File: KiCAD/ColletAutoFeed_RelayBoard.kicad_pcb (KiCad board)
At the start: 2 copper layers, 117.2 x 159.5 mm, 55 parts, among them J1 XW4M-10D2-H1DS, J2 XW4M-02D1-H1DA, K1 G5V-1, K2 G5V-1, K3 G5V-1, K4 G5V-1, K5 G5V-1, K6 G5V-1, K7 G5V-1, K8 G5V-1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

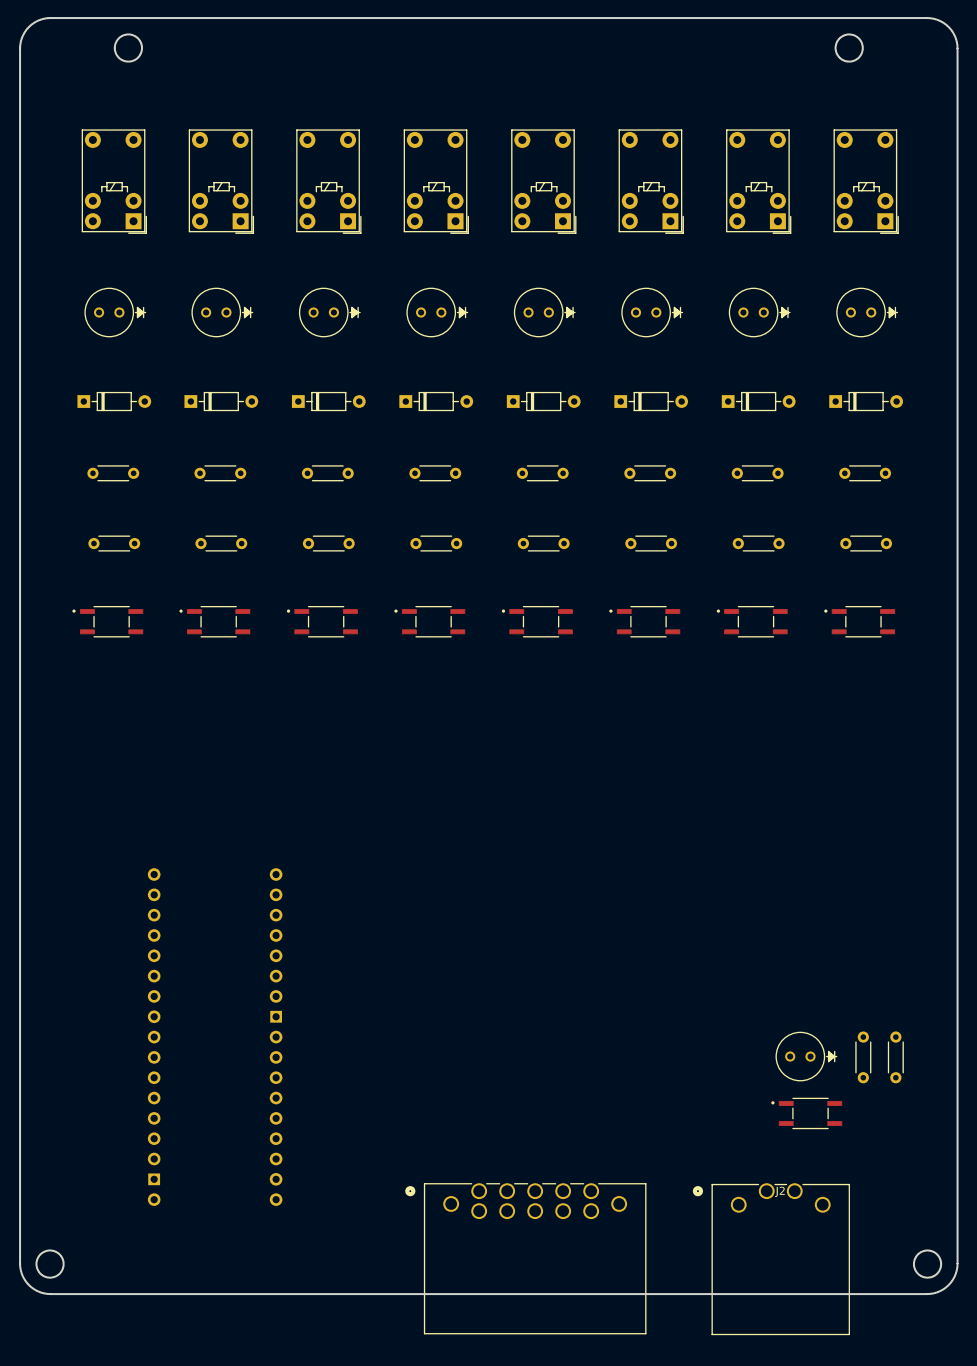
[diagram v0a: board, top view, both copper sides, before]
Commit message: Placed components and routed traces on PCB
Placed components and completed initial routing. Still need to add power and ground planes and figure out silkscreen.
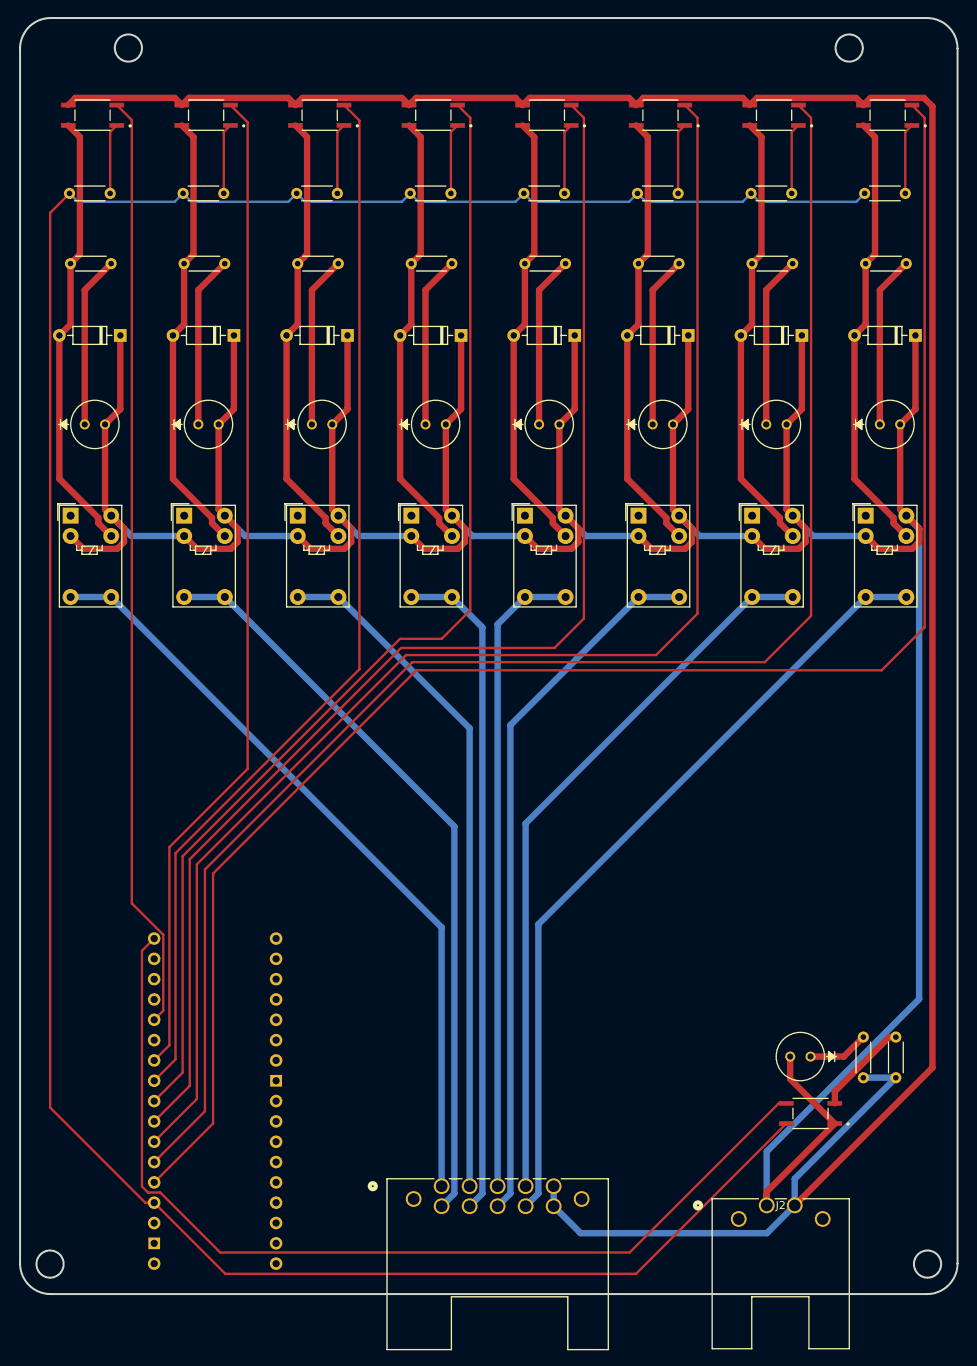
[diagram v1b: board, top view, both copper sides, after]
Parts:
- moved U9 63.4 mm to (143.2, 35.3), turned to 180 degrees
- moved U2 63.4 mm to (43.9, 35.3), turned to 180 degrees
- moved U8 63.4 mm to (129.0, 35.3), turned to 180 degrees
- moved U3 63.3 mm to (58.1, 35.3), turned to 180 degrees
- moved U7 63.3 mm to (114.8, 35.3), turned to 180 degrees
- moved U4 63.3 mm to (72.3, 35.3), turned to 180 degrees
- moved U6 63.3 mm to (100.7, 35.3), turned to 180 degrees
- moved U5 63.3 mm to (86.5, 35.3), turned to 180 degrees
- moved R1 44.5 mm to (41.0, 45.0), turned to 0 degrees
- moved R3 44.4 mm to (55.2, 45.0), turned to 0 degrees
- moved R5 44.3 mm to (69.4, 45.0), turned to 0 degrees
- moved R7 44.1 mm to (83.6, 45.0), turned to 0 degrees
- moved R9 44.1 mm to (97.8, 45.0), turned to 0 degrees
- moved R11 44.0 mm to (112.0, 45.0), turned to 0 degrees
- moved R13 43.9 mm to (126.2, 45.0), turned to 0 degrees
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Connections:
- J1 pad 2: /S2 -> /S3
- J1 pad 3: /S3 -> /S5
- J1 pad 4: /S4 -> /S7
- J1 pad 5: /S5 -> GND
- J1 pad 6: /S6 -> /S2
- J1 pad 7: /S7 -> /S4
- J1 pad 8: /S8 -> /S6
- J1 pad 9: +24V -> /S8
- U2 pad 2: /IO1 -> /IO16
- U3 pad 2: /IO2 -> /IO0
- U4 pad 2: /IO3 -> /IO21
- U5 pad 2: /IO4 -> /IO5
- U6 pad 2: /IO5 -> /IO4
- U7 pad 2: /IO21 -> /IO3
- U8 pad 2: /IO0 -> /IO2
- U9 pad 2: /IO16 -> /IO1
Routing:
- net +24V: track 0.00 -> 472.7 mm
- net /MCU 3.3v: track 0.00 -> 329.1 mm
- net GND: track 0.00 -> 319.3 mm
- net /IO1: track 0.00 -> 209.3 mm
- net /IO2: track 0.00 -> 192.6 mm
- net /IO3: track 0.00 -> 176.7 mm
- net /IO4: track 0.00 -> 161.2 mm
- net /IO5: track 0.00 -> 144.6 mm
- net /IO21: track 0.00 -> 133.4 mm
- net /IO0: track 0.00 -> 125.2 mm
- net /IO12: track 0.00 -> 123.3 mm
- net /IO16: track 0.00 -> 117.2 mm
- net /S8: track 0.00 -> 98.8 mm
- net /S1: track 0.00 -> 95.8 mm
- net /S2: track 0.00 -> 93.8 mm
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
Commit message: Added ground and power planes
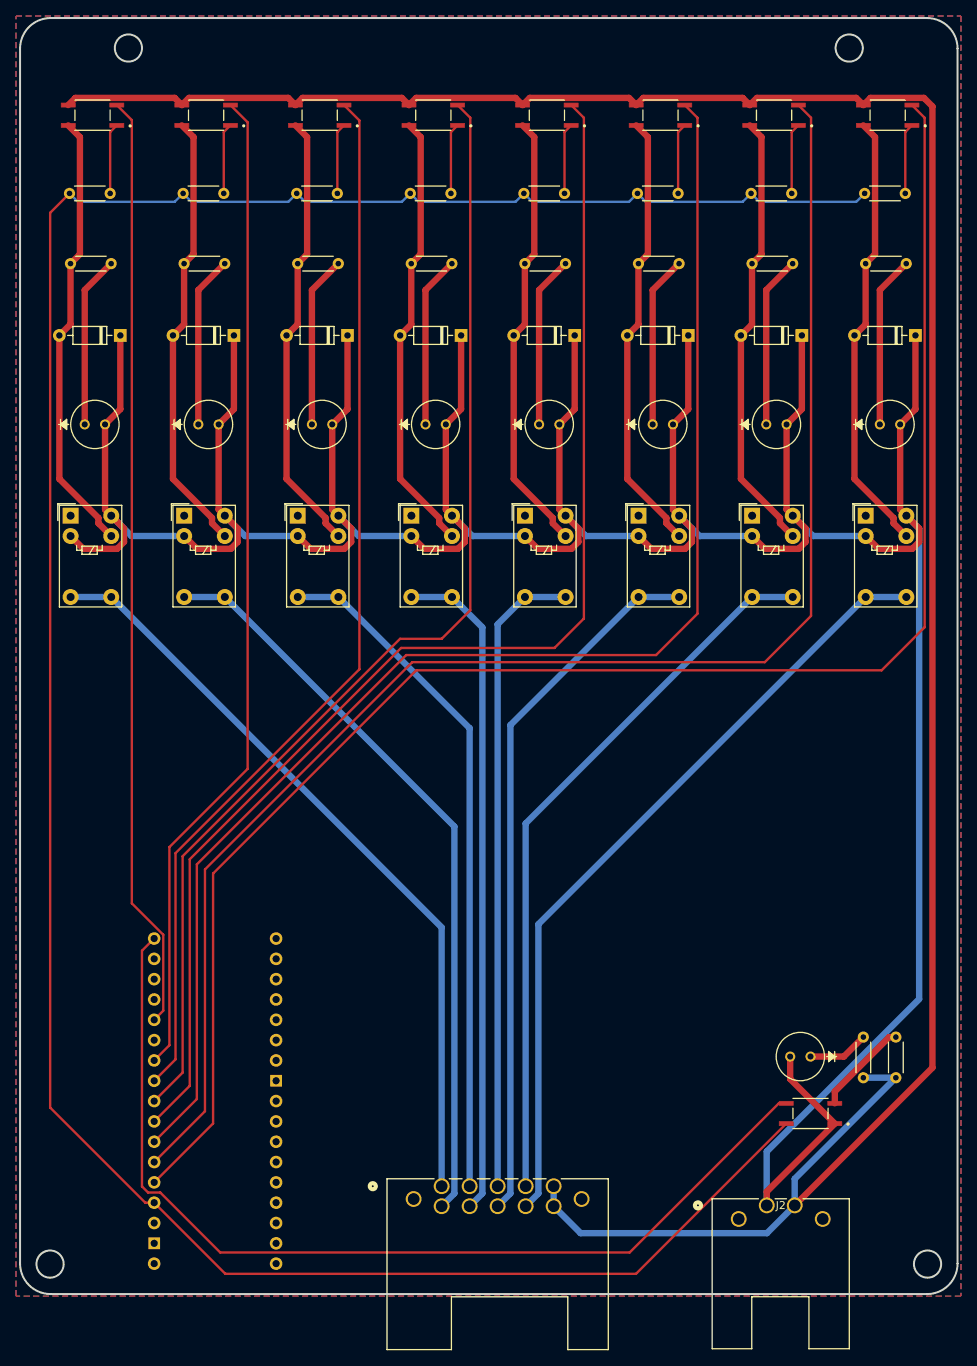
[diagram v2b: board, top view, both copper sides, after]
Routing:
- added copper zone on F.Cu, net +24V
- added copper zone on B.Cu, net GND
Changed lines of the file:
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@@
   (segment (start 133.604 152.931) (end 137.772 152.931) (width 0.8) (layer "F.Cu") (net 78))
   (segment (start 137.772 152.931) (end 140.208 150.495) (width 0.8) (layer "F.Cu") (net 78))
+  (zone (net 1) (net_name "+24V") (layer "F.Cu") (hatch edge 0.5)
+    (priority 1)
+    (connect_pads (clearance 0.5))
+    (min_thickness 0.25) (filled_areas_thickness no)
+    (fill yes (thermal_gap 0.5) (thermal_bridge_width 0.5))
+    (polygon
+      (pts
+        (xy 34.29 22.86)
+        (xy 152.4 22.86)
+        (xy 152.4 182.88)
+        (xy 34.29 182.88)
+      )
+    )
+  )
+  (zone (net 11) (net_name "GND") (layer "B.Cu") (hatch edge 0.5)
+    (connect_pads (clearance 0.5))
+    (min_thickness 0.25) (filled_areas_thickness no)
+    (fill yes (thermal_gap 0.5) (thermal_bridge_width 0.5))
+    (polygon
+      (pts
+        (xy 34.29 22.86)
+        (xy 152.4 22.86)
+        (xy 152.4 182.88)
+        (xy 34.29 182.88)
+      )
+    )
+  )
   (group "" locked (id 1350079e-0e98-4cfe-b8d4-75961c26aff6)
     (members

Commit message: Replaced opto-isolator with through hole version
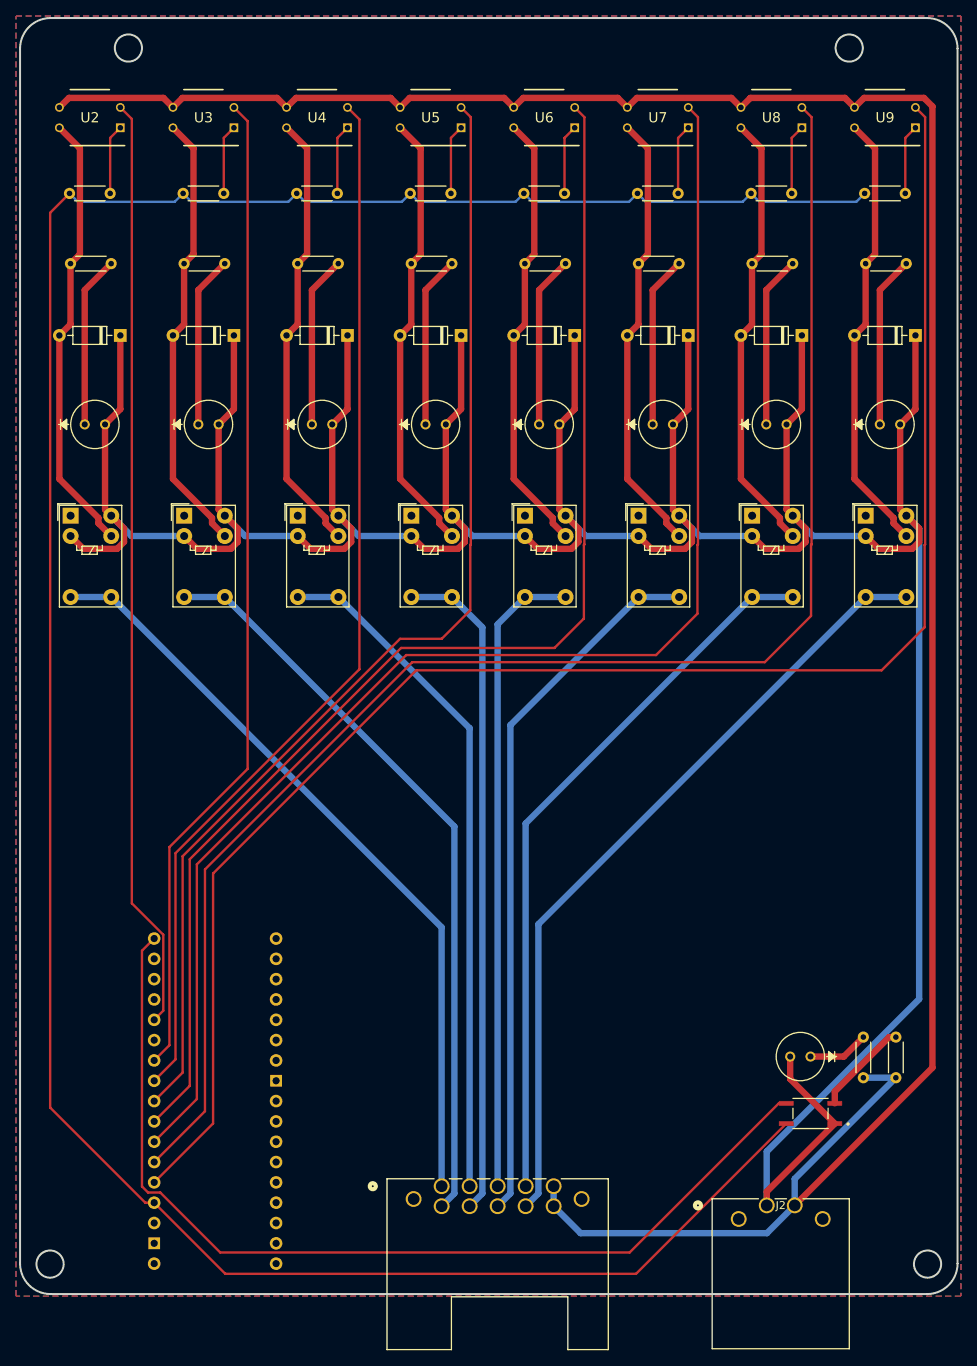
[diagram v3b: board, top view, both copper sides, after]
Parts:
- U2, U3, U4, U5, U6, U7, U8, U9: value PC365NJ0000F -> PC12311NSZ1B; footprint PC365NJ0000F:PC365NJ0000F -> PC12311NSZ1B:PC12311NSZ1B
- moved U4 0.45 mm to (71.9, 35.6)
- moved U7 0.45 mm to (114.5, 35.6)
- moved U8 0.45 mm to (128.7, 35.6)
- moved U9 0.45 mm to (142.9, 35.6)
- moved U2 0.45 mm to (43.5, 35.6)
- moved U3 0.45 mm to (57.7, 35.6)
- moved U5 0.45 mm to (86.1, 35.6)
- moved U6 0.45 mm to (100.3, 35.6)
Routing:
- net GND: track 319.3 -> 322.2 mm
